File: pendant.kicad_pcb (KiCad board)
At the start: 2 copper layers, 35.5 x 51 mm, 7 parts, among them SW3 SW_Push, U1 XIAO-ESP32-S3-DIP

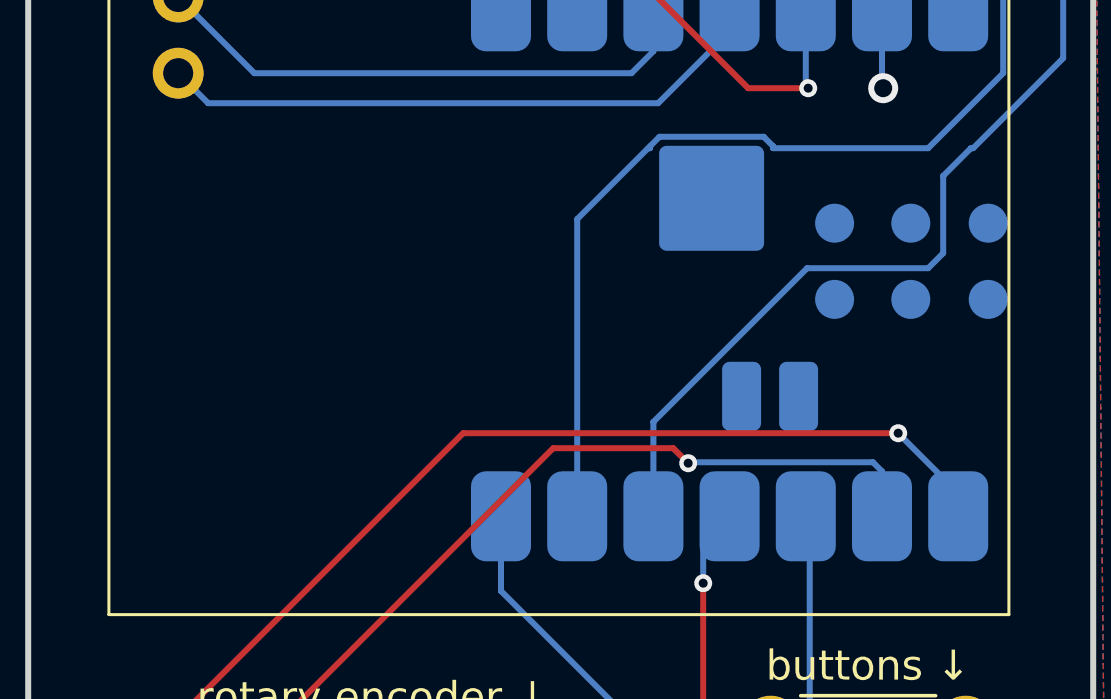
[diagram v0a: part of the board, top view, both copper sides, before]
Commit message: Add battery connector
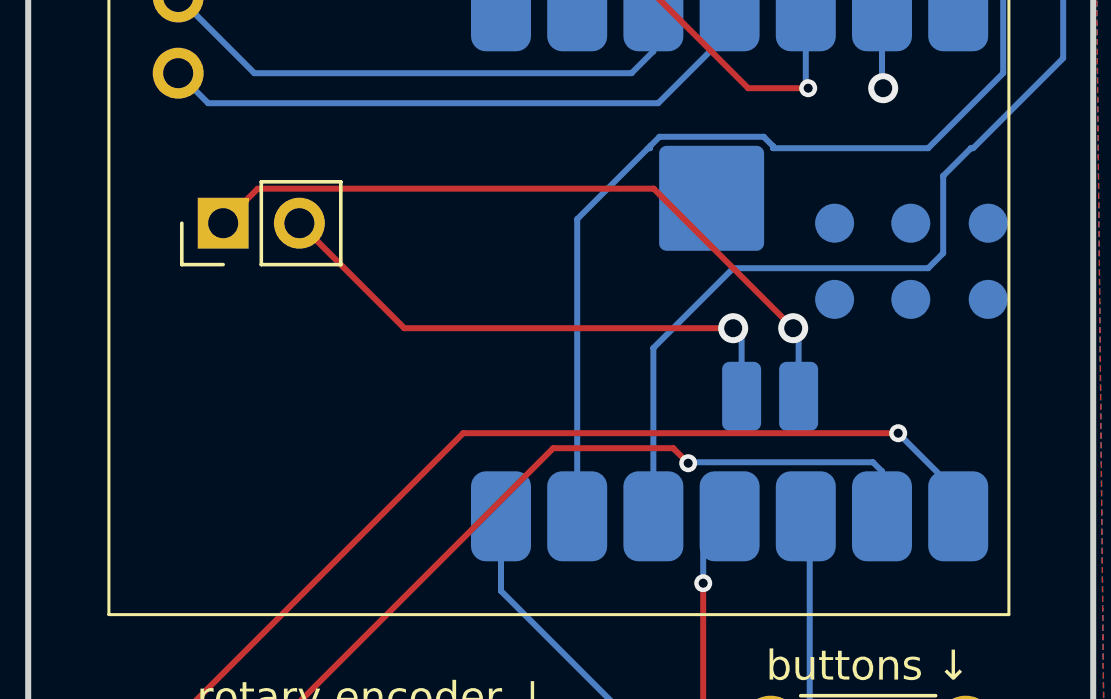
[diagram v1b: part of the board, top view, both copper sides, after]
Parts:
- added battery: PinHeader_1x02_P2.54mm_Vertical, Connector_PinHeader_2.54mm:PinHeader_1x02_P2.54mm_Vertical, F.Cu at (56.5, 67.5)
- extra pins ↓: renamed from extra ↓
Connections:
- U1 pad 16: (no net) -> BAT+
- U1 pad 17: (no net) -> BAT-
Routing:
- net BAT-: track 0.00 -> 23.7 mm, vias 0 -> 1
- net BAT+: track 0.00 -> 18.3 mm, vias 0 -> 1
- net /SDA: track 43.0 -> 44.5 mm
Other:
- board text added: "GND 5V 8 9"

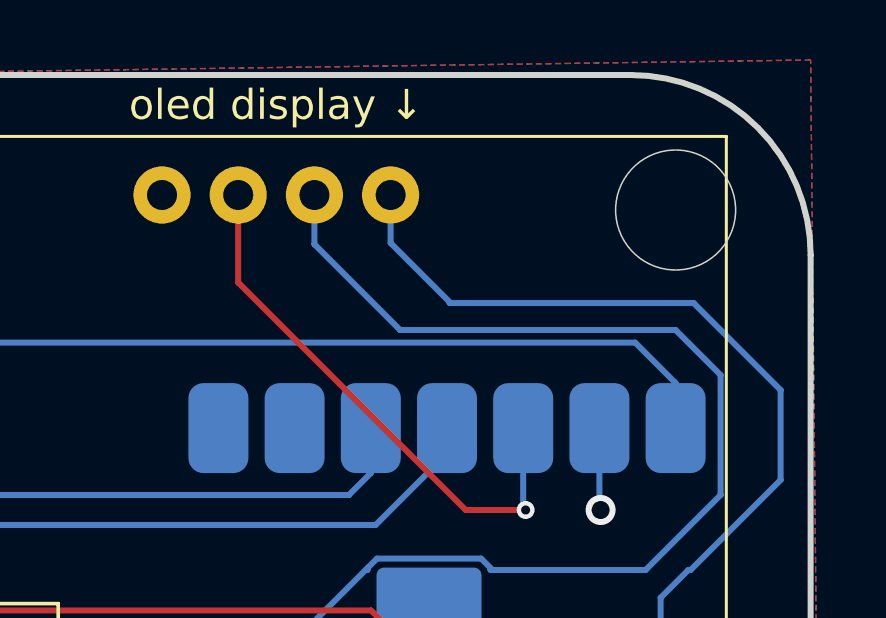
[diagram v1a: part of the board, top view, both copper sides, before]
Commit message: Add battery polarity silkscreen
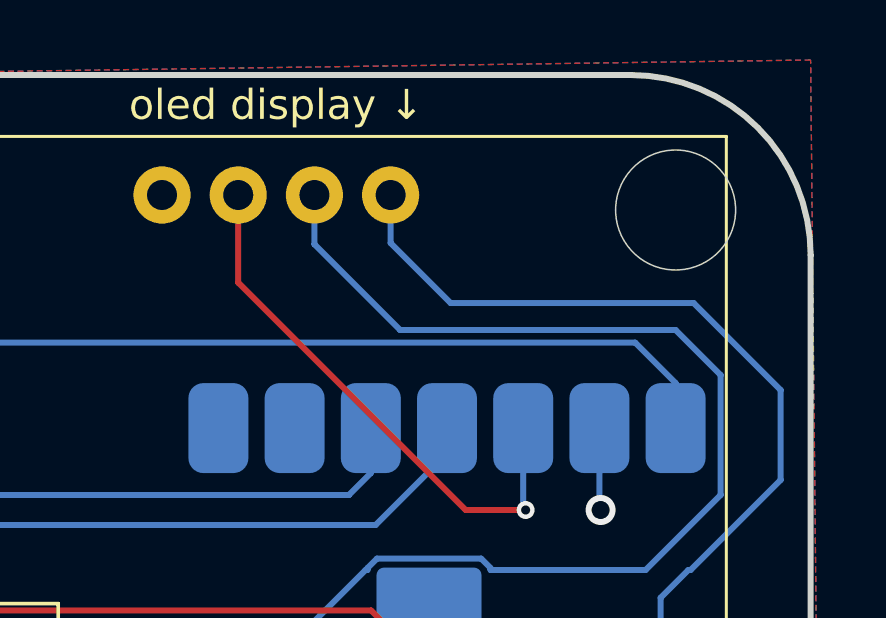
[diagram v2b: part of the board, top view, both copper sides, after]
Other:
- board text added: "- +"
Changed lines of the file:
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@@
 		(tags "Through hole pin header THT 1x02 2.54mm single row")
 		(property "Reference" "battery"
-			(at 0 -2.38 90)
+			(at 0 -2.38 270)
 			(layer "B.SilkS")
 			(effects
@@
 					(thickness 0.15)
 				)
+				(justify mirror)
 			)
 		)
 		(property "Value" "PinHeader_1x02_P2.54mm_Vertical"
 			(at 0 4.92 90)
-			(layer "F.Fab")
+			(layer "B.Fab")
+			(hide yes)
 			(effects
 				(font
@@
 					(thickness 0.15)
 				)
+				(justify mirror)
 			)
 		)
@@
 		)
 	)
+	(gr_text "- +"
+		(at 55.5 69 180)
+		(layer "B.SilkS")
+		(effects
+			(font
+				(size 1.2 1.2)
+				(thickness 0.24)
+				(bold yes)
+			)
+			(justify left bottom mirror)
+		)
+	)
 	(segment
 		(start 74 63)
@@
 		(width 0.2)
 		(layer "B.Cu")
-		(net 2)
-	)
-	(segment
-		(start 73.5 56.101)
-		(end 73.4585 56.101)
-		(width 0.2)
-		(layer "B.Cu")

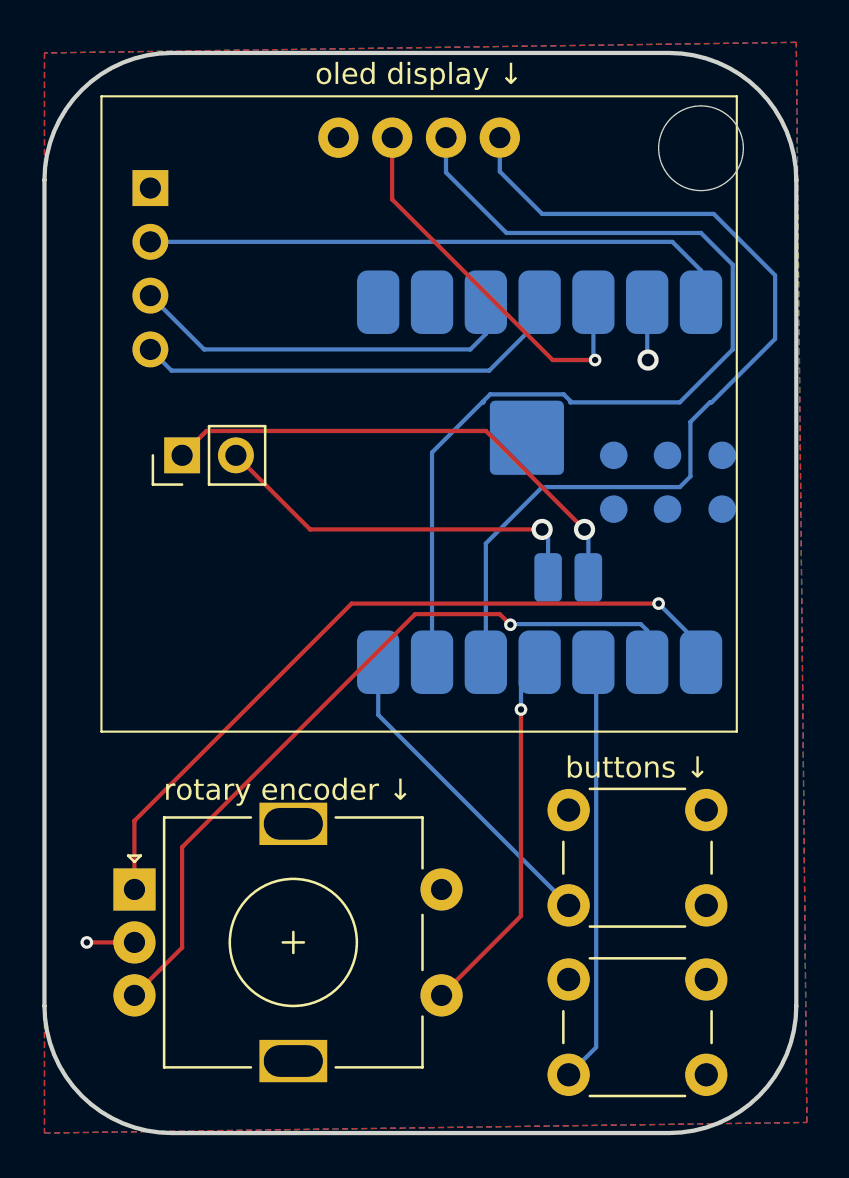
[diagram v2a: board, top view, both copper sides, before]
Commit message: Add SK6812 Mini E LEDs
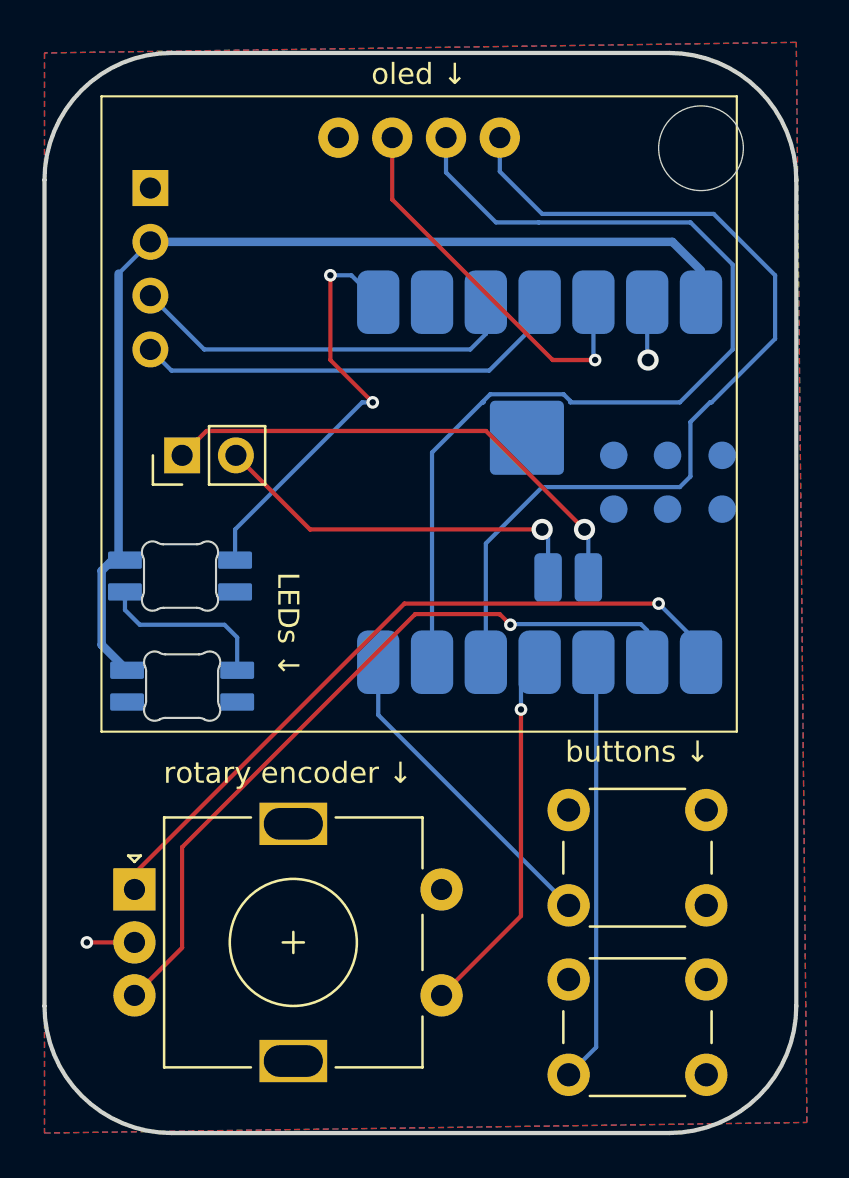
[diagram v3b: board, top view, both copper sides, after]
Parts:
- added D1: SK6812MINI, LED_SMD:SK6812MINI-E_fixed, F.Cu at (56.4, 73.3)
- added D2: SK6812MINI, LED_SMD:SK6812MINI-E_fixed, F.Cu at (56.5, 78.5)
- extra pins ↓: value extra pins -> Extra Pins
- oled ↓: renamed from oled display ↓
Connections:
- U1 pad 8: unconnected-(U1-GPIO44_D7_RX-Pad8) -> /LED_GPIO
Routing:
- net +5V: track 28.1 -> 50.2 mm
- net /LED_GPIO: track 0.00 -> 20.0 mm, vias 0 -> 2
- net Net-(D1-DOUT): track 0.00 -> 8.24 mm
- net /EC_GPIO_A: track 35.8 -> 34.4 mm
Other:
- board text added: "LEDs ↓"

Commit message: Add soup
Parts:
- removed the G*** at (60.5, 52.0)
- added G***: LOGO, LOGO, B.Cu at (62.0, 90.0)
- added G***: LOGO, LOGO, B.Cu at (76.0, 51.5)
